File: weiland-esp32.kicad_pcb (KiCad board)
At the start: 2 copper layers, 24 x 47 mm, 19 parts, among them J2 Conn_01x06_Pin, J3 Conn_01x04_Pin, J4 Conn_01x04_Pin, U1 ESP32-WROOM-32E(8MB), U2 AMS1117-3.3_C347222, U3 GR6205-SOP-8, U4 MAX98357AEWL_T

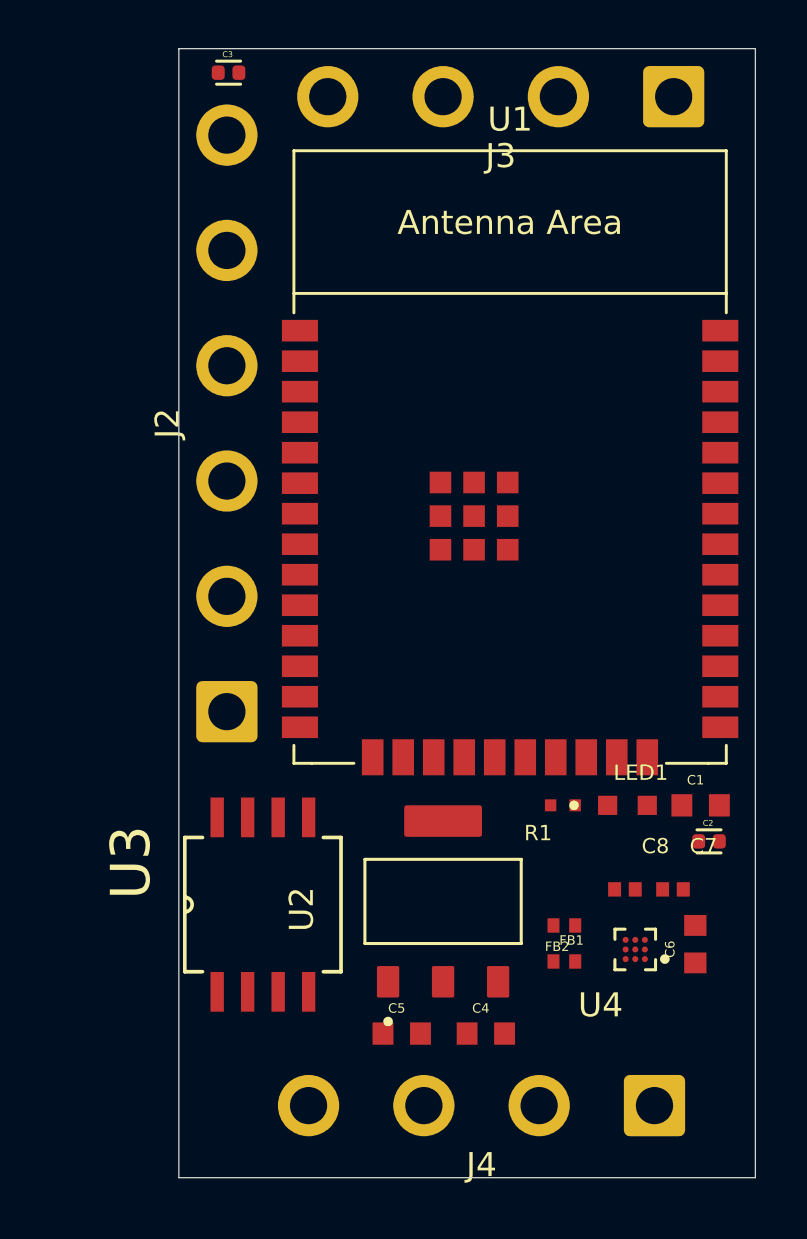
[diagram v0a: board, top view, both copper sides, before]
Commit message: antenna can't be on the board itself (interference)
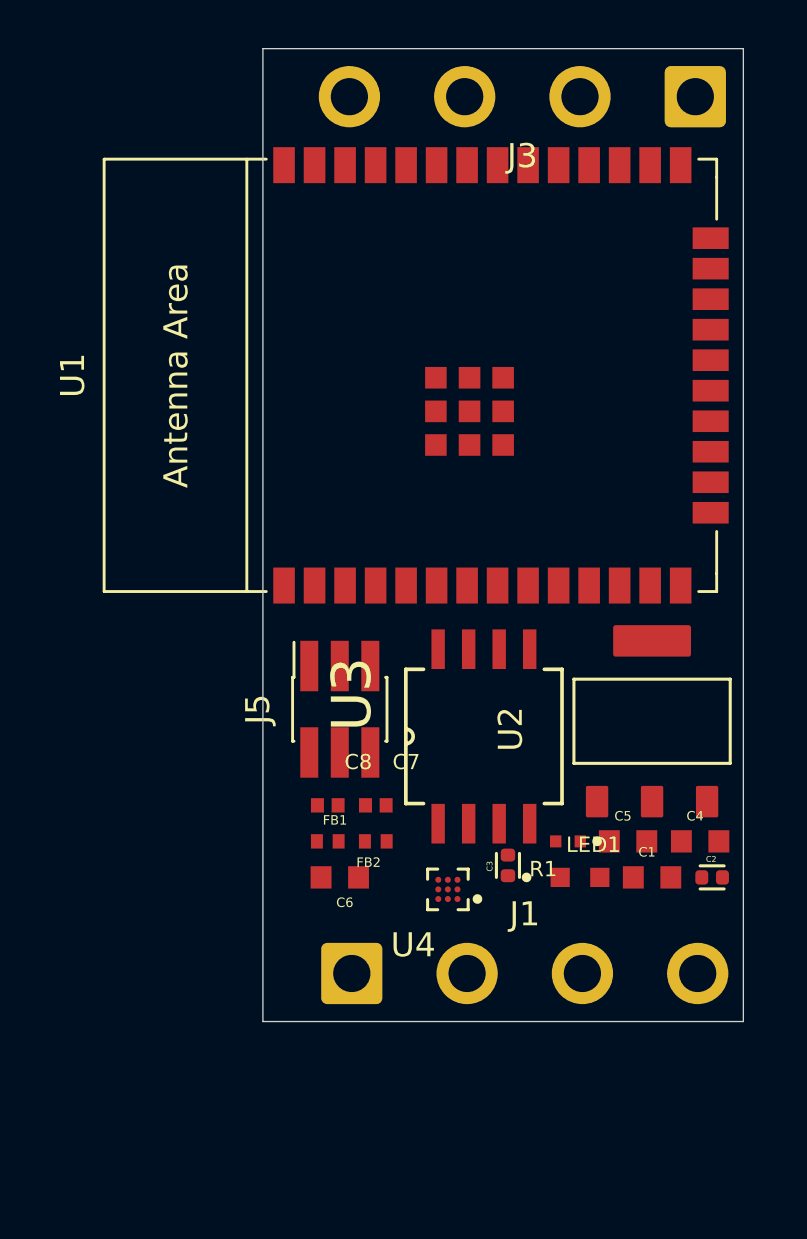
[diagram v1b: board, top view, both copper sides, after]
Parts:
- removed J2: Conn_01x06_Pin, Connector_Wire:SolderWire-0.75sqmm_1x06_P4.8mm_D1.25mm_OD2.3mm
- removed J4: Conn_01x04_Pin, Connector_Wire:SolderWire-0.75sqmm_1x04_P4.8mm_D1.25mm_OD2.3mm
- added J1: Conn_01x04_Pin, Connector_Wire:SolderWire-0.75sqmm_1x04_P4.8mm_D1.25mm_OD2.3mm, F.Cu at (131.2, 117.5)
- added J5: Conn_02x03_Odd_Even, Connector_PinSocket_1.27mm:PinSocket_2x03_P1.27mm_Vertical_SMD, F.Cu at (130.7, 106.5)
- moved C3 35.0 mm to (137.7, 113.0), turned to 90 degrees
- moved C6 15.1 mm to (130.7, 113.5), turned to 180 degrees
- moved C7 12.9 mm to (132.2, 110.5)
- moved C8 12.9 mm to (130.2, 110.5)
- moved C5 12.4 mm to (142.7, 112.0)
- moved C4 12.0 mm to (145.7, 112.0)
- moved U3 11.6 mm to (136.7, 107.6)
- moved U2 11.5 mm to (143.7, 107.0)
- moved FB1 11.0 mm to (130.2, 112.0)
- moved FB2 8.59 mm to (132.2, 112.0)
- moved U4 8.19 mm to (135.2, 114.0)
- moved U1 5.68 mm to (135.4, 92.6), turned to 90 degrees
- moved C1 3.62 mm to (143.7, 113.5)
- moved LED1 3.59 mm to (140.7, 113.5)
- moved R1 1.51 mm to (140.2, 112.0)
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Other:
- board size 24 x 47 mm -> 20 x 40.5 mm

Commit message: routing draft completed
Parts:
- removed J3: Conn_01x04_Pin, Connector_Wire:SolderWire-0.75sqmm_1x04_P4.8mm_D1.25mm_OD2.3mm
- added J2: Conn_01x05_Pin, customlibrary:SolderWire-0.75sqmm_1x05_P4.8mm_D1.25mm_OD2.3mm, F.Cu at (149.0, 117.5)
- moved J1 39.0 mm to (145.0, 81.0), turned to 180 degrees
- moved C1 18.1 mm to (129.0, 103.0)
- moved C2 18.1 mm to (131.5, 103.0)
- moved C4 16.5 mm to (129.5, 115.0)
- moved FB1 15.6 mm to (145.5, 115.0)
- moved J5 13.3 mm to (144.0, 106.0)
- moved C5 13.3 mm to (129.5, 113.5)
- moved C8 12.8 mm to (143.0, 111.5), turned to 90 degrees
- moved U2 12.8 mm to (131.0, 108.5)
- moved FB2 11.7 mm to (143.5, 115.0)
- moved C7 11.2 mm to (143.0, 113.5), turned to 90 degrees
- moved U4 10.4 mm to (145.5, 112.5)
- moved C3 6.53 mm to (143.5, 110.0), turned to 180 degrees
- moved C6 5.89 mm to (136.5, 112.5), turned to 0 degrees
- moved R1 4.17 mm to (136.5, 113.9)
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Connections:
- C3 pad 2: +5V_EXT -> +5V
- J5 pad 2: +5V_EXT -> +5V
- U4 pad A1: unconnected-(U4-SD_MODE-PadA1) -> +5V
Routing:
- net GND: track 0.00 -> 104.8 mm, vias 0 -> 4
- net /OUTN: track 0.00 -> 46.2 mm, vias 0 -> 6
- net /OUTP: track 0.00 -> 44.6 mm, vias 0 -> 2
- net /RXD0: track 0.00 -> 32.6 mm, vias 0 -> 2
- net /TXD0: track 0.00 -> 32.5 mm, vias 0 -> 2
- net +5V: track 0.00 -> 32.4 mm, vias 0 -> 2
- net /OUTA: track 0.00 -> 31.6 mm, vias 0 -> 1
- net /IO0: track 0.00 -> 26.6 mm, vias 0 -> 2
- net /EN: track 0.00 -> 22.5 mm, vias 0 -> 2
- net +3V3: track 0.00 -> 21.4 mm, vias 0 -> 2
- net /IO25: track 0.00 -> 20.6 mm
- net /IO26: track 0.00 -> 13.1 mm, vias 0 -> 2
- net /IO27: track 0.00 -> 13.0 mm, vias 0 -> 2
- net /OUTB: track 0.00 -> 11.6 mm, vias 0 -> 1
- net Net-(U4-OUTN): track 0.00 -> 3.06 mm
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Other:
- board size 20 x 40.5 mm -> 20.3 x 40.5 mm
